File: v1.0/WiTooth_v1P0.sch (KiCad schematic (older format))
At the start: 47 parts, among them P1 USB_A_MALE, P4 CONN_01X20, P5 CONN_01X20, Q1 2N3904-MMBT, Q2 2N3904-MMBT, SW1 RESET, SW2 BOOT, SW3 USER_SW, U1 AMS1117-3V3, U2 CP2102, U3 ESP-32_WROOM32_Rectangle, Y1 Crystal

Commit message: Added images folder; schematic verified
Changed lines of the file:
@@
 LIBS:crystal-new
 LIBS:usb_a_male_pcb
-LIBS:4n35_opto
-LIBS:24MHz
-LIBS:0850bm14e0016
-LIBS:2450BM14G0011
-LIBS:antenna_2.4GHz
-LIBS:cc1310_7x7
-LIBS:cc1310_7x7_new
-LIBS:cc2650
-LIBS:cc2650_7x7
-LIBS:connectors
-LIBS:crystal_24MHz
-LIBS:df08s1_bridge_rec-ic
-LIBS:edge_sma
-LIBS:esp-12e
-LIBS:esp-32_wroom32_Exact
-LIBS:henlv_5v_2a
-LIBS:henlv-ac220s3_3dcs-3w
-LIBS:HM-10
-LIBS:ic-cpu
-LIBS:ic-io
-LIBS:ic-misc
-LIBS:ic-power
-LIBS:inductor
-LIBS:inductor_L
-LIBS:lp5907_ldo_250ma
-LIBS:ltr-303als
-LIBS:Micro_USB_B
-LIBS:passive
-LIBS:PROBE
-LIBS:RFM_module
-LIBS:sfm-110-02-s-d-a-k-tr
-LIBS:si7006
-LIBS:switch_dpdt
-LIBS:switch_spdt
-LIBS:switches
-LIBS:tps782
-LIBS:tps63051
-LIBS:triac_board
-LIBS:vbus053az
-LIBS:xbee
-LIBS:WiTooth_v1P0-cache
 EELAYER 25 0
 EELAYER END
@@
 Sheet 1 1
 Title "WiTooth"
-Date ""
+Date "2017-02-17"
 Rev "v1.0"
 Comp ""
@@
 Text Notes 5250 5375 0    39   ~ 0
 Should be made as break-away section
-Text Notes 1925 2500 0    79   ~ 0
+Text Notes 1875 2700 0    79   ~ 0
 Programming Section
 $Comp

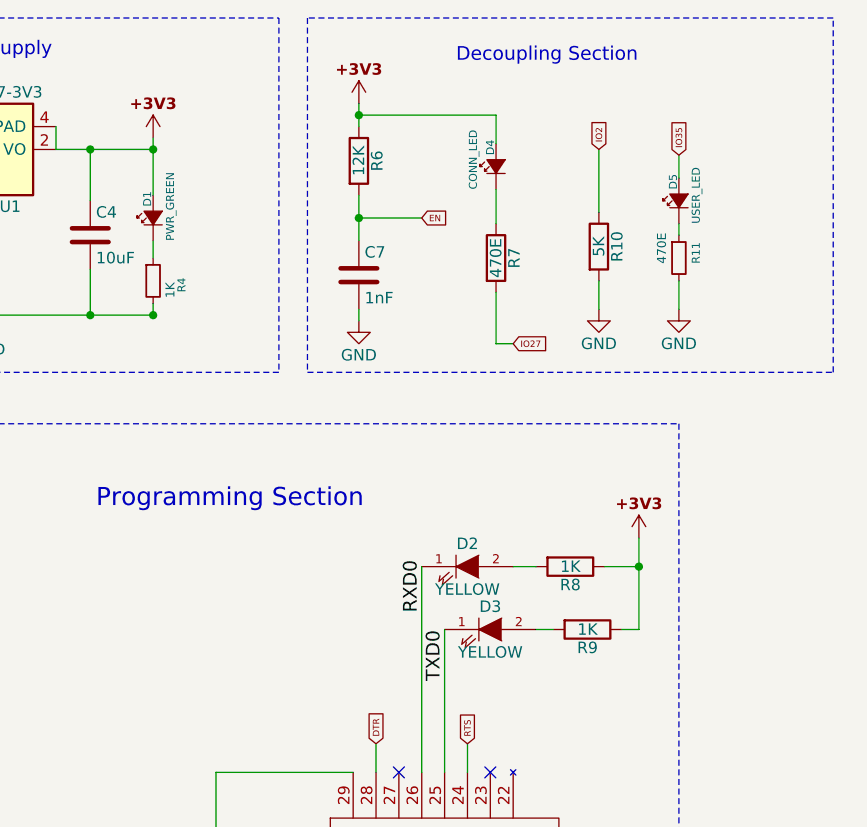
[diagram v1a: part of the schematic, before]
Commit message: verified layout; ready for fab
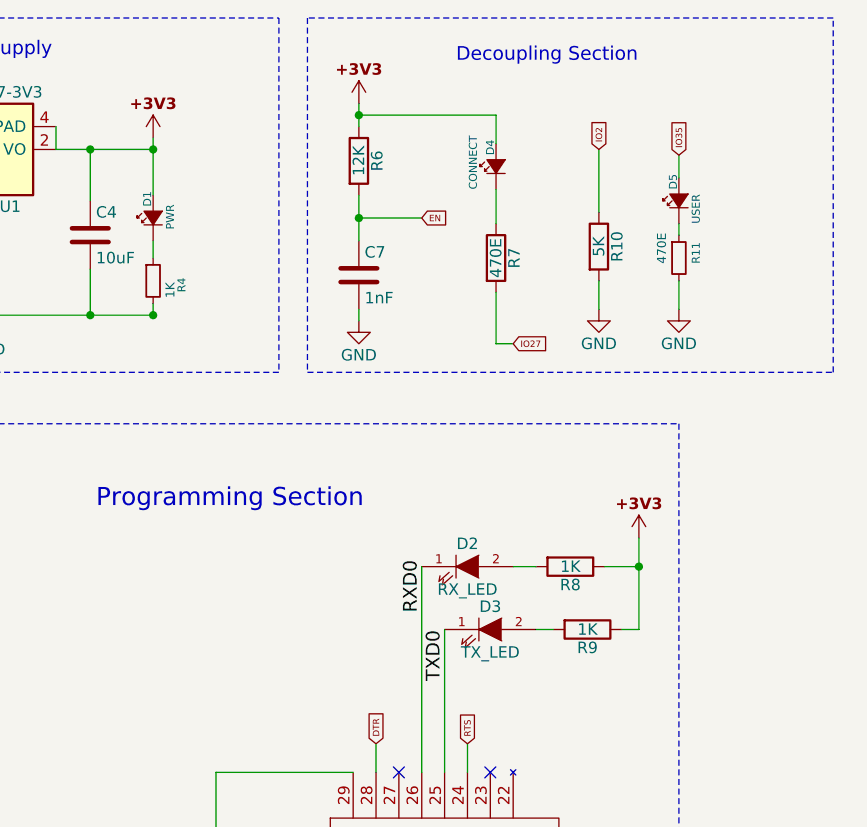
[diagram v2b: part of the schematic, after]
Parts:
- D1: value PWR_GREEN -> PWR
- D2: value YELLOW -> RX_LED
- D3: value YELLOW -> TX_LED
- D4: value CONN_LED -> CONNECT
- D5: value USER_LED -> USER
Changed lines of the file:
@@
 P 2125 1425
 F 0 "D1" H 2175 1450 35  0000 L CNN
-F 1 "PWR_GREEN" H 2025 1350 35  0000 L CNN
+F 1 "PWR" H 2075 1350 35  0000 L CNN
 F 2 "LEDs:LED_0805" V 2125 1425 50  0001 C CNN
 F 3 "" V 2125 1425 50  0000 C CNN
@@
 P 4425 1350
 F 0 "D5" H 4475 1375 35  0000 L CNN
-F 1 "USER_LED" H 4325 1275 35  0000 L CNN
+F 1 "USER" H 4325 1275 35  0000 L CNN
 F 2 "LEDs:LED_0805" V 4425 1350 50  0001 C CNN
 F 3 "" V 4425 1350 50  0000 C CNN
@@
 P 3625 1200
 F 0 "D4" H 3675 1225 35  0000 L CNN
-F 1 "CONN_LED" H 3525 1300 35  0000 L CNN
+F 1 "CONNECT" H 3525 1300 35  0000 L CNN
 F 2 "LEDs:LED_0805" V 3625 1200 50  0001 C CNN
 F 3 "" V 3625 1200 50  0000 C CNN
@@
 P 3600 3225
 F 0 "D3" H 3600 3325 50  0000 C CNN
-F 1 "YELLOW" H 3600 3125 50  0000 C CNN
+F 1 "TX_LED" H 3600 3125 50  0000 C CNN
 F 2 "LEDs:LED_0805" H 3600 3225 50  0001 C CNN
 F 3 "" H 3600 3225 50  0000 C CNN
@@
 P 3500 2950
 F 0 "D2" H 3500 3050 50  0000 C CNN
-F 1 "YELLOW" H 3500 2850 50  0000 C CNN
+F 1 "RX_LED" H 3500 2850 50  0000 C CNN
 F 2 "LEDs:LED_0805" H 3500 2950 50  0001 C CNN
 F 3 "" H 3500 2950 50  0000 C CNN

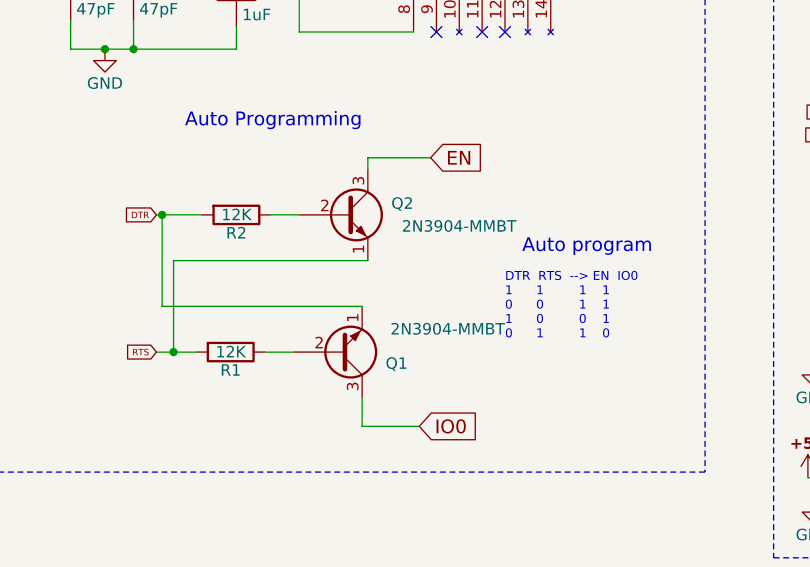
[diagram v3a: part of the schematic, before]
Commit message: updated the 2N3904 npn transistor footprint
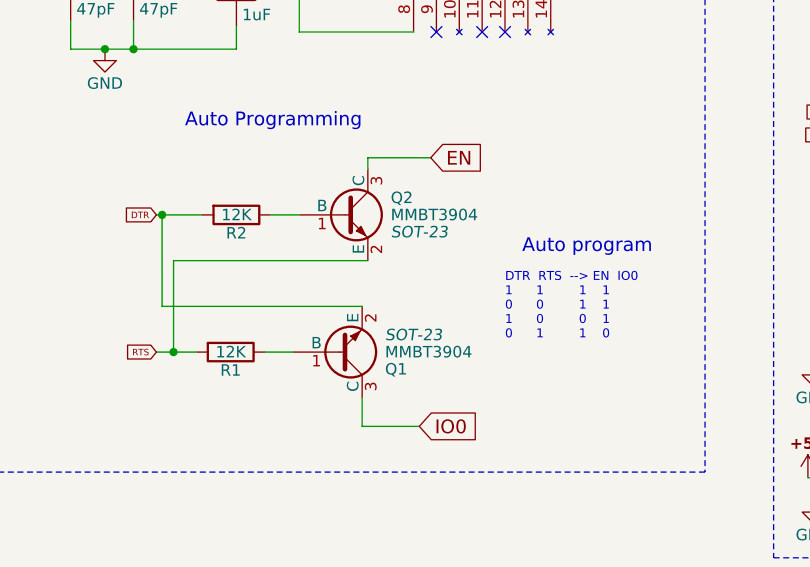
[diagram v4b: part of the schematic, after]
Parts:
- removed Q1, Q2: 2N3904-MMBT, TO_SOT_Packages_SMD:SOT-23_Handsoldering, symbol Q_NPN_EBC
- added Q1, Q2: MMBT3904, SOT-23, symbol MMBT3904
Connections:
- net DTR: now also Q1.2 (E)
- net EN: now also Q2.3 (C)
- net IO0: now also Q1.3 (C)
- net RTS: now also Q2.2 (E)
- net at R2.1: now also Q2.1 (B)
- net at R1.1: now also Q1.1 (B)
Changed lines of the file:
@@
-$EndComp
-$Comp
-L Q_NPN_EBC Q2
-U 1 1 589A127B
-P 2850 6250
-F 0 "Q2" H 3150 6300 50  0000 R CNN
-F 1 "2N3904-MMBT" H 3600 6200 50  0000 R CNN
-F 2 "TO_SOT_Packages_SMD:SOT-23_Handsoldering" H 3050 6350 50  0001 C CNN
-F 3 "" H 2850 6250 50  0000 C CNN
-	1    2850 6250
-	1    0    0    -1
 $EndComp
 $Comp
@@
 	1    2350 6850
 	0    1    1    0
-$EndComp
-$Comp
-L Q_NPN_EBC Q1
-U 1 1 589A13CF
-P 2825 6850
-F 0 "Q1" H 3125 6900 50  0000 R CNN
-F 1 "2N3904-MMBT" H 3550 6750 50  0000 R CNN
-F 2 "TO_SOT_Packages_SMD:SOT-23_Handsoldering" H 3025 6950 50  0001 C CNN
-F 3 "" H 2825 6850 50  0000 C CNN
-	1    2825 6850
-	1    0    0    1
 $EndComp
 Text GLabel 2025 6850 0    28   Input ~ 0
@@
 Connection ~ 1500 4350
 Connection ~ 2400 4350
+$Comp
+L MMBT3904 Q2
+U 1 1 58AD737C
+P 2850 6250
+F 0 "Q2" H 3050 6325 50  0000 L CNN
+F 1 "MMBT3904" H 3050 6250 50  0000 L CNN
+F 2 "SOT-23" H 3050 6175 50  0000 L CIN
+F 3 "" H 2850 6250 50  0000 L CNN
+	1    2850 6250
+	1    0    0    -1
+$EndComp
+$Comp
+L MMBT3904 Q1
+U 1 1 58AD88EE
+P 2825 6850
+F 0 "Q1" H 3025 6925 50  0000 L CNN
+F 1 "MMBT3904" H 3025 6850 50  0000 L CNN
+F 2 "SOT-23" H 3025 6775 50  0000 L CIN
+F 3 "" H 2825 6850 50  0000 L CNN
+	1    2825 6850
+	1    0    0    1
+$EndComp
 $EndSCHEMATC
